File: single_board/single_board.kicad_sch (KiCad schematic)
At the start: 110 parts, among them J1 CAN_OUT, J10 SPI Debug, J11 Screw_Terminal_01x02, J12 BOOTSEL, J13 Conn_01x03, J14 Conn_01x04, J15 Screw_Terminal_01x02, J16 Conn_01x03, J17 Conn_01x04, J18 UART, J19 Conn_01x03, J2 USB_C_Receptacle_USB2.0_16P, J20 Conn_01x04, J21 Screw_Terminal_01x02, J22 Conn_01x03, J23 Conn_01x04, J24 Conn_01x05, J25 Conn_01x02, J26 490107670612, J3 Screw_Terminal_01x03, J4 Conn_01x03, J5 Screw_Terminal_01x02, J6 Conn_01x04, J7 Screw_Terminal_01x02, J8 Conn_01x03, J9 Conn_01x04, Q1 2N7002, SW1 Button, U1 AP2112K-3.3, U2 TJA1042T-3, U3 USBLC6-2SC6, U4 LSM6DSV, U5 STM32G474VBTx, Y1 FC-135

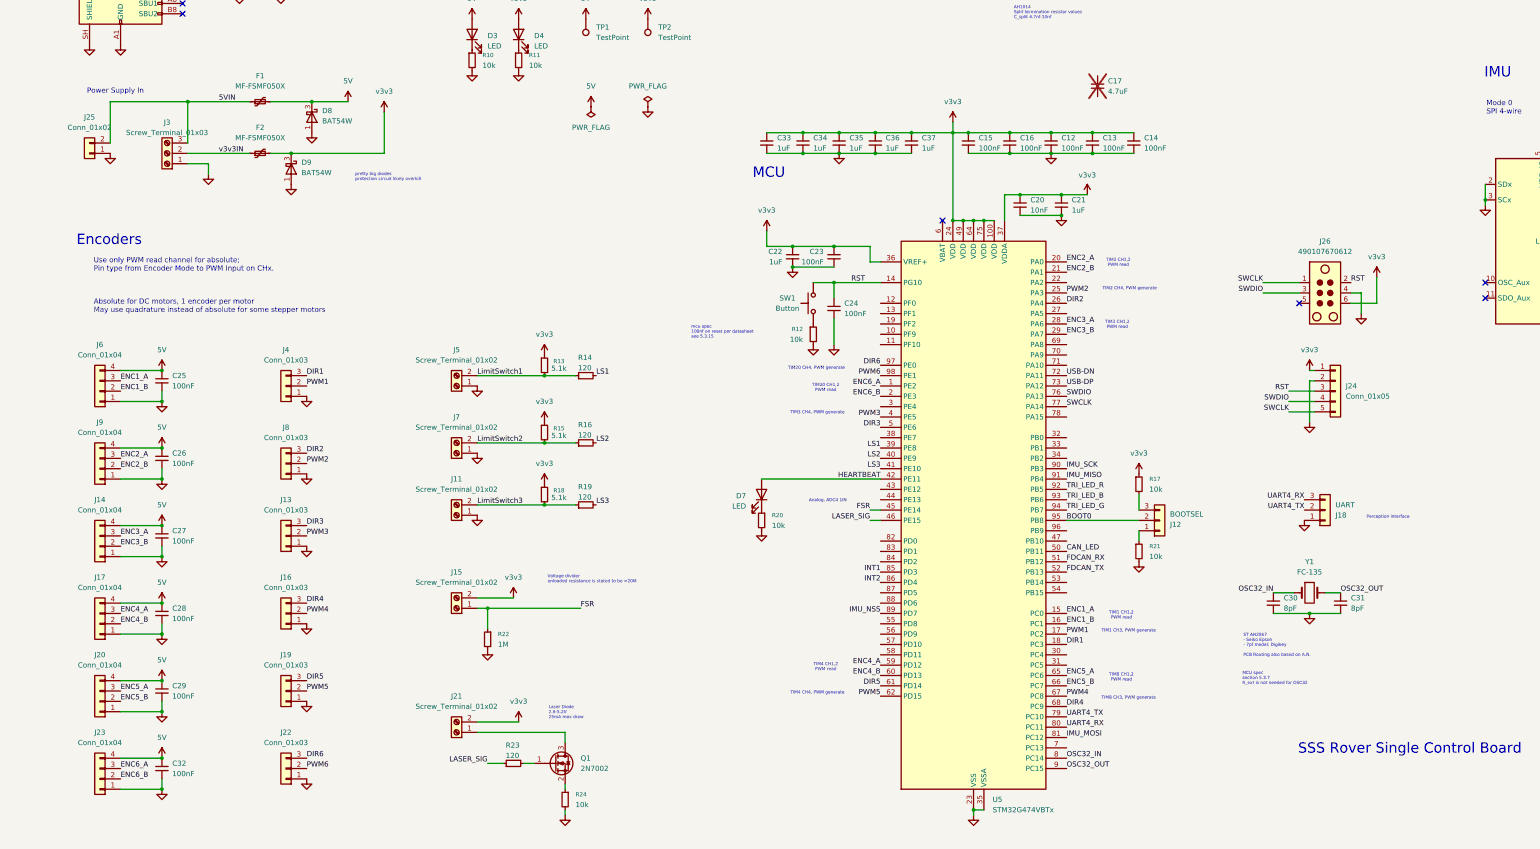
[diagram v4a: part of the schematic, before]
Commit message: Edit pin headers
Pinout optimized for encoders
High side p-mos for fsr input
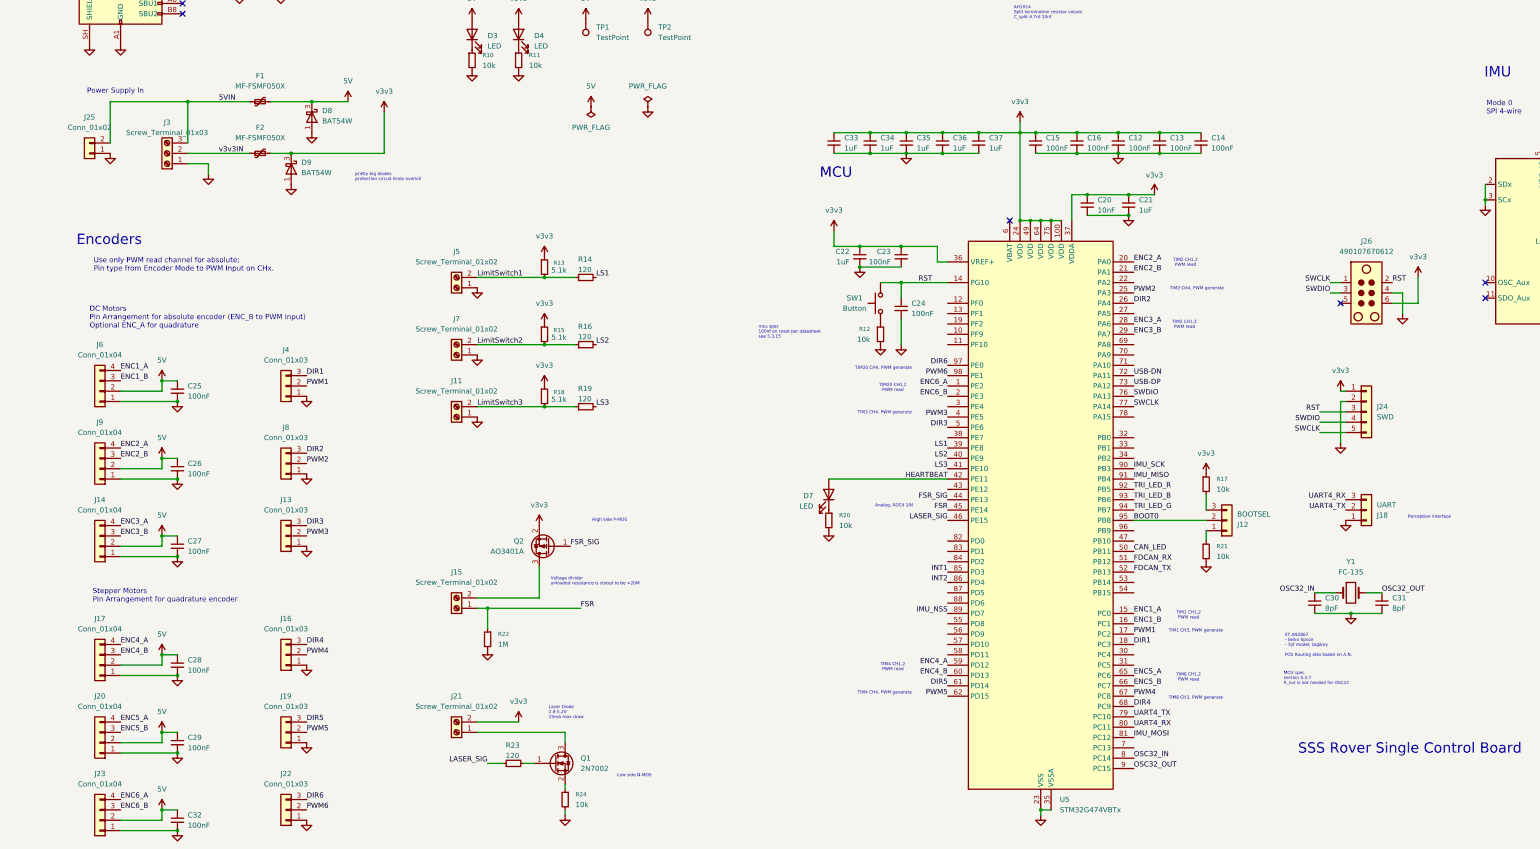
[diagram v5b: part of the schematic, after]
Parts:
- removed C17: 4.7uF, Capacitor_SMD:C_0603_1608Metric, symbol Device:C_Small
- added Q2: AO3401A, Package_TO_SOT_SMD:SOT-23, symbol Transistor_FET:AO3401A
- J24: value Conn_01x05 -> SWD
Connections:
- net 5V: now also J14.2 (Pin_2), J17.2 (Pin_2), J20.2 (Pin_2), J23.2 (Pin_2), J6.2 (Pin_2), J9.2 (Pin_2); no longer J14.4 (Pin_4), J17.4 (Pin_4), J20.4 (Pin_4), J23.4 (Pin_4), J6.4 (Pin_4), J9.4 (Pin_4)
- net ENC1_A: now also J6.4 (Pin_4); no longer J6.3 (Pin_3)
- net ENC1_B: now also J6.3 (Pin_3); no longer J6.2 (Pin_2)
- net ENC2_A: now also J9.4 (Pin_4); no longer J9.3 (Pin_3)
- net ENC2_B: now also J9.3 (Pin_3); no longer J9.2 (Pin_2)
- net ENC3_A: now also J14.4 (Pin_4); no longer J14.3 (Pin_3)
- net ENC3_B: now also J14.3 (Pin_3); no longer J14.2 (Pin_2)
- net ENC4_A: now also J17.4 (Pin_4); no longer J17.3 (Pin_3)
- net ENC4_B: now also J17.3 (Pin_3); no longer J17.2 (Pin_2)
- net ENC5_A: now also J20.4 (Pin_4); no longer J20.3 (Pin_3)
- net ENC5_B: now also J20.3 (Pin_3); no longer J20.2 (Pin_2)
- net ENC6_A: now also J23.4 (Pin_4); no longer J23.3 (Pin_3)
- net ENC6_B: now also J23.3 (Pin_3); no longer J23.2 (Pin_2)
- net v3v3: now also Q2.2 (S); no longer J15.2 (Pin_2)
- net FSR_SIG: now reaches U5.44 (PE13)
- net FSR_SIG: now also Q2.1 (G)
- new net: J15.2 (Pin_2), Q2.3 (D)
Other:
- note added: "DC Motors Pin Arrangement for absolute encoder (ENC_B to PWM input) Optional ENC_A for quadrature"
- note added: "High side P-MOS"
- note added: "Low side N-MOS"
- note added: "Stepper Motors Pin Arrangement for quadrature encoder"
- note removed: "Absolute for DC motors, 1 encoder per motor May use quadrature instead of absolute for some stepper motors"
- moved on the sheet: C12, C13, C14, C15, C16, C20, C21, C22, C23, C24, C25, C30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

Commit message: Fix Laser and FSR switches
Appropriate pull up/down resistors
Remove in line resistors
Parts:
- removed R23: 120, Resistor_SMD:R_0402_1005Metric_Pad0.72x0.64mm_HandSolder, symbol Device:R_Small
- added R22: 10k, Resistor_SMD:R_0402_1005Metric_Pad0.72x0.64mm_HandSolder, symbol Device:R_Small
- renumbered C18 to C12, C19 to C13, C33 to C14, C34 to C15, C35 to C16, C36 to C17, C37 to C18, C15 to C19, C16 to C20, C12 to C21, C13 to C22, C14 to C23, C20 to C24, C21 to C25, C22 to C26, C23 to C27, C24 to C28, C25 to C29, C26 to C30, C27 to C31, C30 to C32, C31 to C33, C28 to C34, C29 to C35, C32 to C36, D8 to D5, D9 to D6, J7 to J11, J8 to J12, J9 to J13, J11 to J14, J18 to J15, J12 to J16, J13 to J17, J14 to J18, J16 to J19, J15 to J20, J17 to J21, J19 to J22, J20 to J23, J21 to J24, J22 to J25, J23 to J26, J25 to J3, J3 to J4, J26 to J5, J5 to J6, J4 to J7, J6 to J8, J24 to J9, Q2 to Q1, Q1 to Q2, R13 to R12, R12 to R13, R18 to R17, R19 to R18, R17 to R19, R22 to R23
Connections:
- net FSR_SIG: now also R22.1
- net GND: now also Q2.2 (S)
- net LASER_SIG: now also Q2.1 (G), R24.1
- net v3v3: now also R22.2
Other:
- note added: "GPIO-Low : FSR powered Can read with adc"
- note added: "GPIO-Low : Laser off"
- note added: "Limit Switches, Laser, Force Sensor"
- moved on the sheet: J11, J14, J20, J24, J5, J6, Q1, Q2, R12, R14, R15, R16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

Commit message: P-Mos reverse polarity protection
removed fuse and schottky diode
shrink bom, keep reverse polarity protection on 5v and 3.3v lines
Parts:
- removed D5, D6: BAT54W, Package_TO_SOT_SMD:SOT-323_SC-70, symbol Diode:BAT54W
- removed F1, F2: MF-FSMF050X, Fuse:Fuse_0603_1608Metric_Pad1.05x0.95mm_HandSolder, symbol Device:Polyfuse_Small
- added Q3, Q4, Q5: AO3401A, Package_TO_SOT_SMD:SOT-23, symbol Transistor_FET:AO3401A
- added R25, R26, R27: 10k, Resistor_SMD:R_0402_1005Metric_Pad0.72x0.64mm_HandSolder, symbol Device:R_Small
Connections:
- net 5V: now also Q3.2 (S)
- net 5VIN: now also Q3.3 (D)
- net GND: now also R25.2, R26.2, R27.2
- net v3v3: now also Q4.2 (S), Q5.2 (S); no longer J5.6, J9.1 (Pin_1)
- net v3v3IN: now also J5.6, J9.1 (Pin_1), Q4.3 (D), Q5.3 (D)
- new net: Q4.1 (G), R26.1
- new net: Q3.1 (G), R25.1
- new net: Q5.1 (G), R27.1
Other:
- note added: "Reverse input protection"
- note removed: "pretty big diodes protection circuit likely overkill"
- moved on the sheet: J3, J4

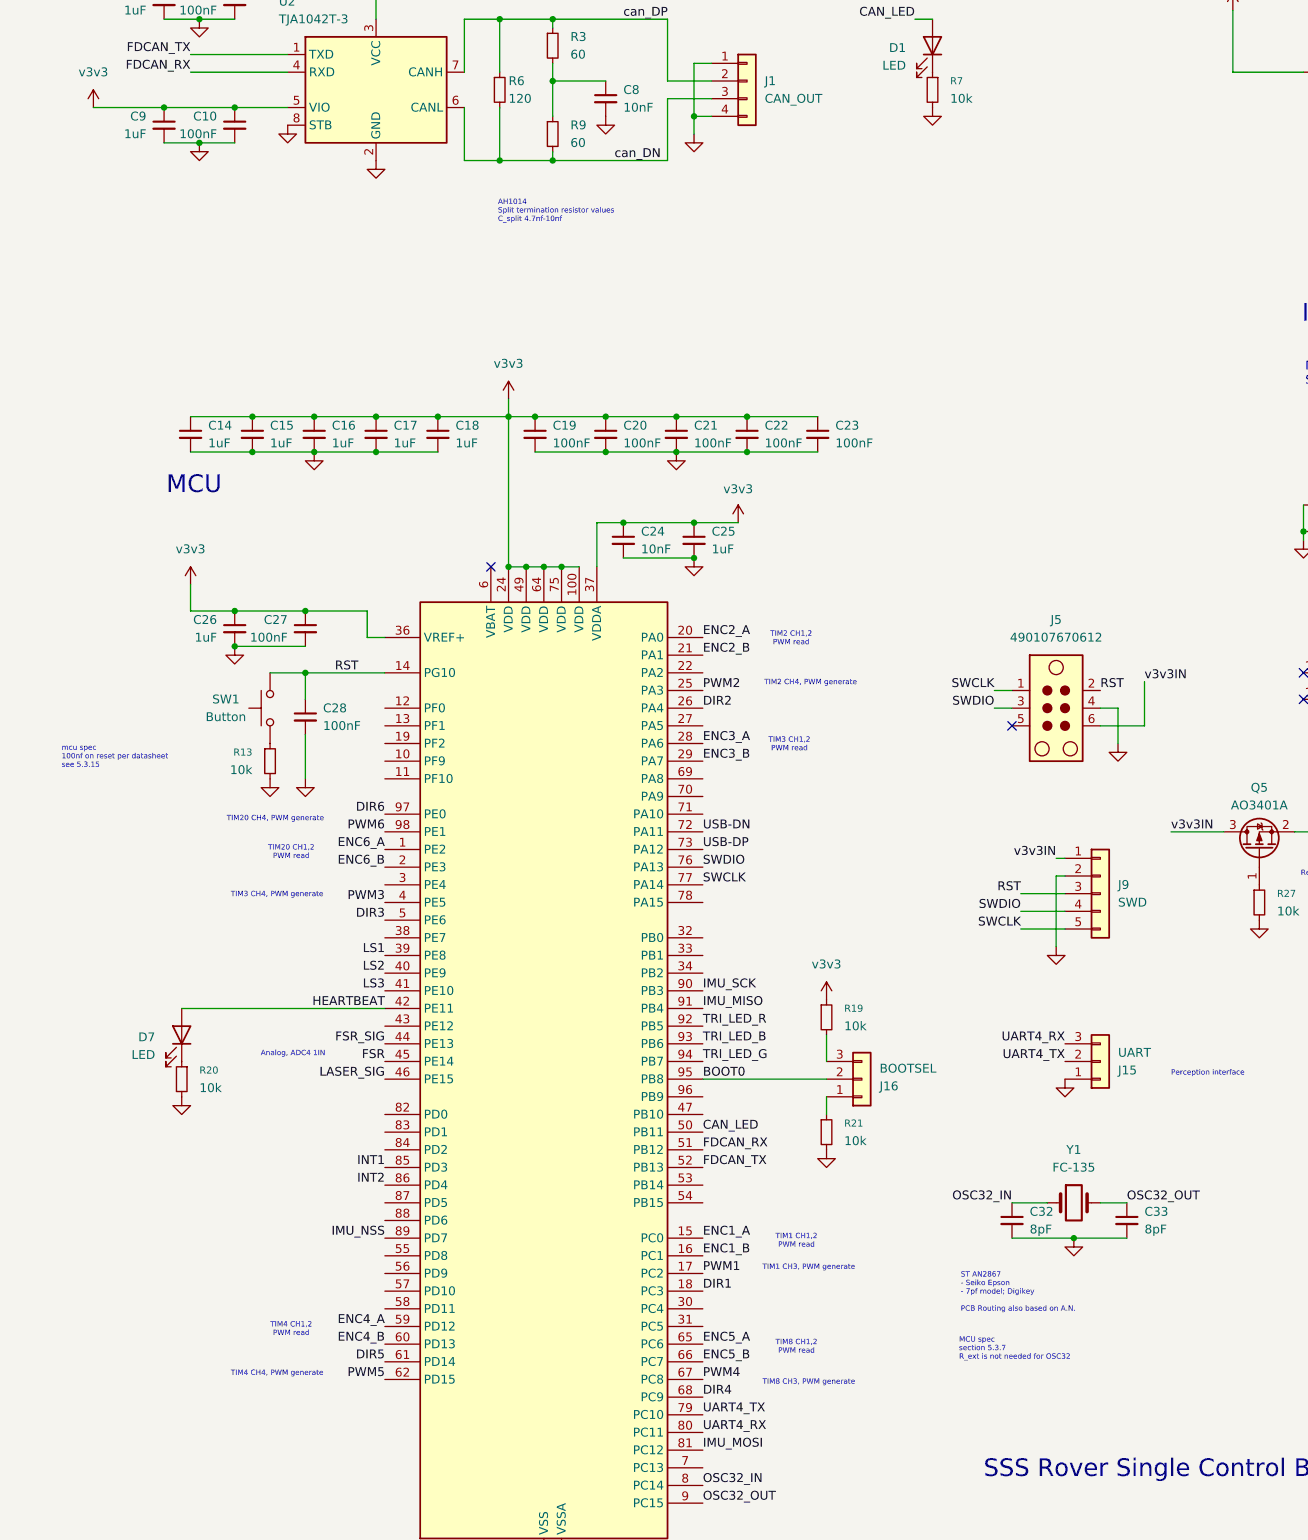
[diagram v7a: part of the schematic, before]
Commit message: Rough Placement
changes to schematic:
8pf to 10pf on crystal
2.54mm pitch screw terminals
can standby pin
shuffle other pinouts
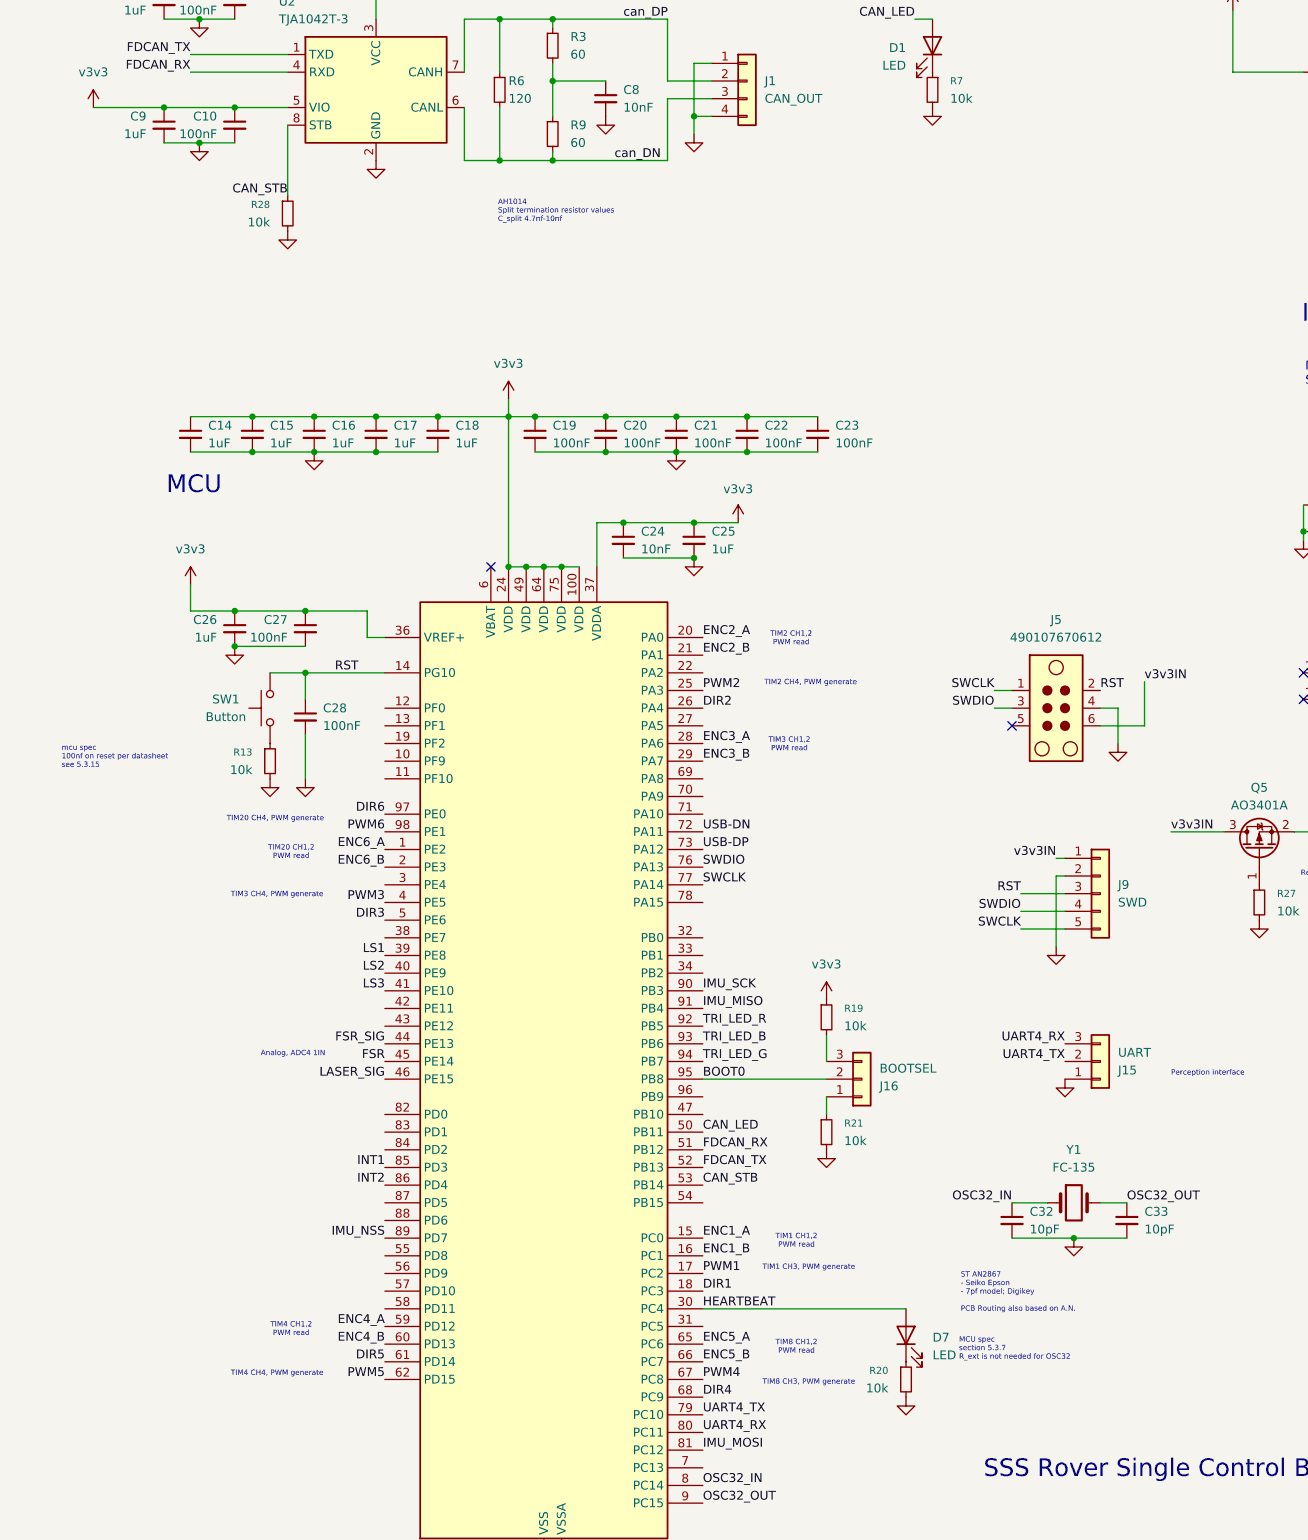
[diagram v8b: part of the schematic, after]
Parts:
- added R28: 10k, Resistor_SMD:R_0402_1005Metric_Pad0.72x0.64mm_HandSolder, symbol Device:R_Small
- C32, C33: value 8pF -> 10pF
- J11, J14, J20, J24, J6: footprint TerminalBlock:TerminalBlock_MaiXu_MX126-5.0-02P_1x02_P5.00mm -> TerminalBlock:TerminalBlock_Xinya_XY308-2.54-2P_1x02_P2.54mm_Horizontal
- J4: footprint TerminalBlock:TerminalBlock_MaiXu_MX126-5.0-03P_1x03_P5.00mm -> TerminalBlock:TerminalBlock_Xinya_XY308-2.54-3P_1x03_P2.54mm_Horizontal
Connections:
- net GND: now also R28.2; no longer U2.8 (STB)
- net HEARTBEAT: now also U5.30 (PC4); no longer U5.42 (PE11)
- net CAN_STB: now reaches U5.53 (PB14)
- net CAN_STB: now also U2.8 (STB), R28.1
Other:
- moved on the sheet: D7, R20
